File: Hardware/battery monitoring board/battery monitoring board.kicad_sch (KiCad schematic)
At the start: 1 part

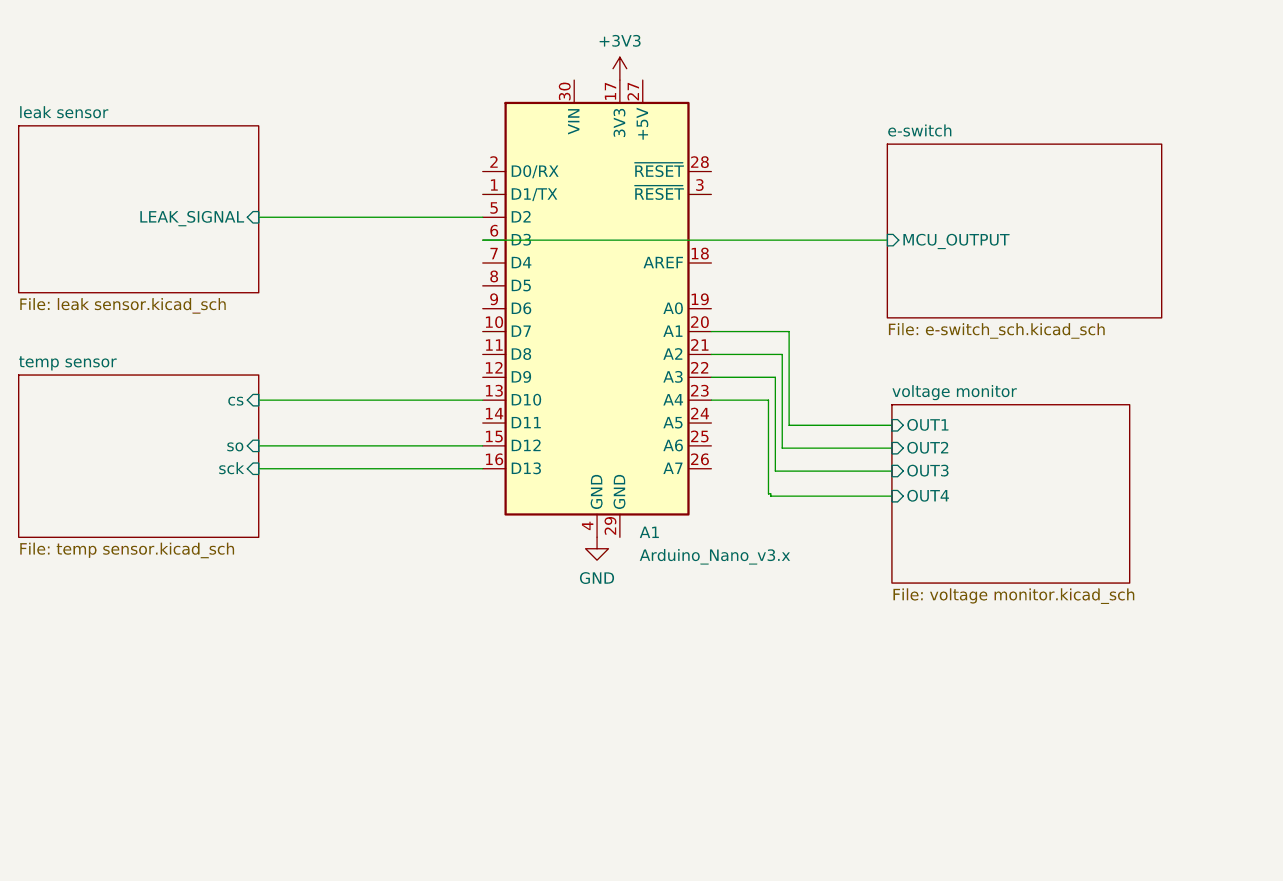
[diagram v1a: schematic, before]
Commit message: Added second battery monitor
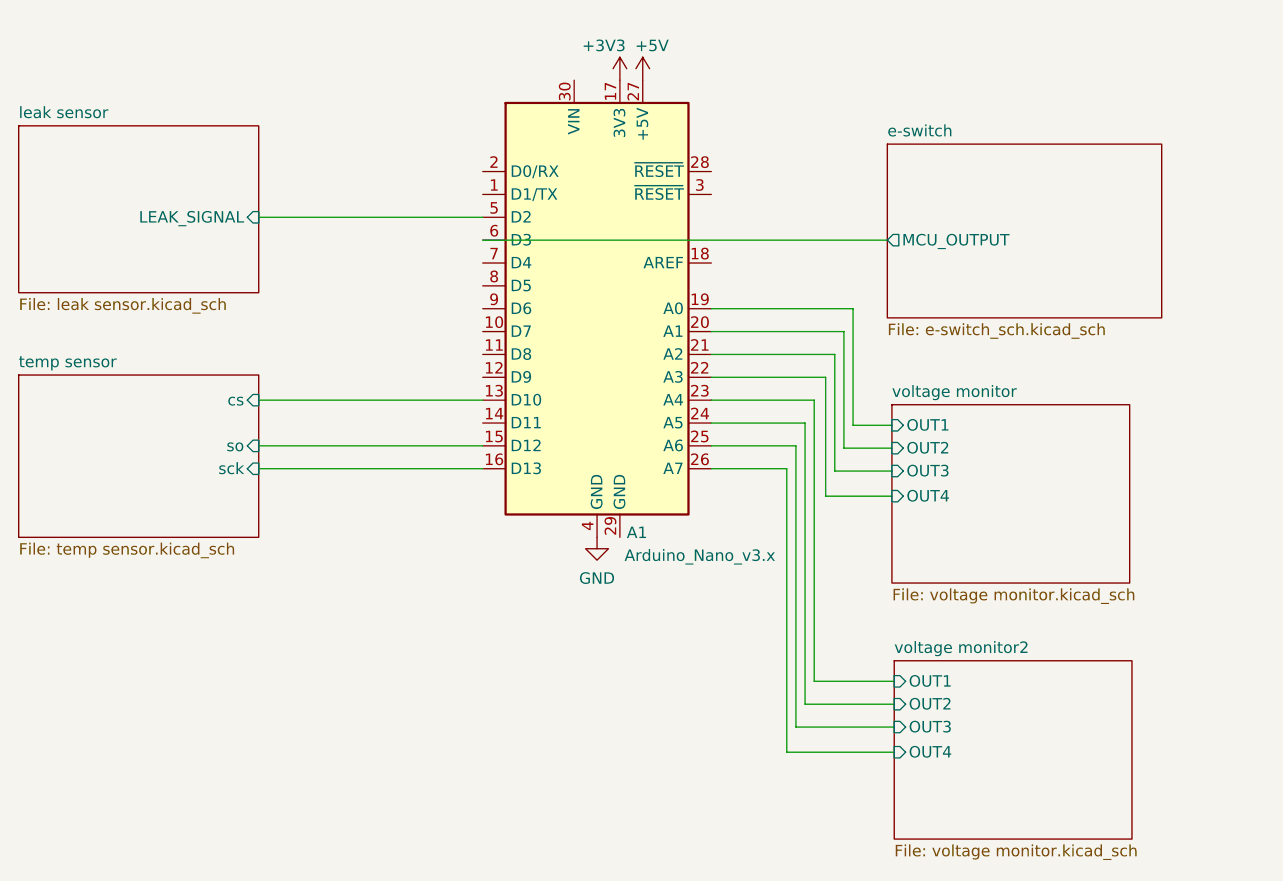
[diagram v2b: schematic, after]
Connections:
- net voltage monitor/OUT1: now also A1.19 (A0); no longer A1.20 (A1)
- net voltage monitor/OUT2: now also A1.20 (A1); no longer A1.21 (A2)
- net voltage monitor/OUT3: now also A1.21 (A2); no longer A1.22 (A3)
- net voltage monitor/OUT4: now also A1.22 (A3); no longer A1.23 (A4)
- net voltage monitor2/OUT2: now reaches A1.24 (A5)
- net voltage monitor2/OUT3: now reaches A1.25 (A6)
- net voltage monitor2/OUT4: now reaches A1.26 (A7)
- net +5V: now reaches A1.27 (+5V)
- new net voltage monitor2/OUT1: A1.23 (A4)
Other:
- added sheet voltage monitor2 (voltage monitor.kicad_sch)
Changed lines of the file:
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@@
 (kicad_sch (version 20230121) (generator eeschema)
   (paper "A4")
-  (wire (pts (xy 154.178 103.632) (xy 141.224 103.632))
+  (wire (pts (xy 148.844 88.138) (xy 134.112 88.138))
     (stroke (width 0) (type default))
   )
@@
     (stroke (width 0) (type default))
   )
-  (wire (pts (xy 140.462 106.172) (xy 140.462 95.758))
-    (stroke (width 0) (type default))
-  )
-  (wire (pts (xy 154.178 101.092) (xy 141.986 101.092))
-    (stroke (width 0) (type default))
-  )
-  (wire (pts (xy 141.986 101.092) (xy 141.986 90.678))
-    (stroke (width 0) (type default))
-  )
-  (wire (pts (xy 141.224 93.218) (xy 134.112 93.218))
-    (stroke (width 0) (type default))
-  )
-  (wire (pts (xy 140.716 106.426) (xy 154.178 106.426))
-    (stroke (width 0) (type default))
-  )
-  (wire (pts (xy 134.112 95.758) (xy 140.462 95.758))
+  (wire (pts (xy 149.86 85.598) (xy 149.86 98.552))
+    (stroke (width 0) (type default))
+  )
+  (wire (pts (xy 134.112 93.218) (xy 146.812 93.218))
+    (stroke (width 0) (type default))
+  )
+  (wire (pts (xy 147.828 90.678) (xy 147.828 103.632))
     (stroke (width 0) (type default))
   )
@@
     (stroke (width 0) (type default))
   )
-  (wire (pts (xy 154.178 98.552) (xy 142.748 98.552))
+  (wire (pts (xy 143.51 100.838) (xy 143.51 132.08))
     (stroke (width 0) (type default))
   )
@@
     (stroke (width 0) (type default))
   )
-  (wire (pts (xy 140.716 106.172) (xy 140.462 106.172))
-    (stroke (width 0) (type default))
-  )
-  (wire (pts (xy 141.224 103.632) (xy 141.224 93.218))
-    (stroke (width 0) (type default))
-  )
-  (wire (pts (xy 142.748 98.552) (xy 142.748 88.138))
-    (stroke (width 0) (type default))
-  )
-  (wire (pts (xy 140.716 106.172) (xy 140.716 106.426))
+  (wire (pts (xy 145.542 127) (xy 145.542 95.758))
+    (stroke (width 0) (type default))
+  )
+  (wire (pts (xy 148.844 101.092) (xy 148.844 88.138))
+    (stroke (width 0) (type default))
+  )
+  (wire (pts (xy 134.112 100.838) (xy 143.51 100.838))
+    (stroke (width 0) (type default))
+  )
+  (wire (pts (xy 134.112 98.298) (xy 144.526 98.298))
+    (stroke (width 0) (type default))
+  )
+  (wire (pts (xy 134.112 103.378) (xy 142.494 103.378))
+    (stroke (width 0) (type default))
+  )
+  (wire (pts (xy 134.112 90.678) (xy 147.828 90.678))
+    (stroke (width 0) (type default))
+  )
+  (wire (pts (xy 154.432 127) (xy 145.542 127))
+    (stroke (width 0) (type default))
+  )
+  (wire (pts (xy 147.828 103.632) (xy 154.178 103.632))
+    (stroke (width 0) (type default))
+  )
+  (wire (pts (xy 154.178 101.092) (xy 148.844 101.092))
+    (stroke (width 0) (type default))
+  )
+  (wire (pts (xy 146.812 106.426) (xy 154.178 106.426))
+    (stroke (width 0) (type default))
+  )
+  (wire (pts (xy 149.86 98.552) (xy 154.178 98.552))
+    (stroke (width 0) (type default))
+  )
+  (wire (pts (xy 144.526 129.54) (xy 154.432 129.54))
+    (stroke (width 0) (type default))
+  )
+  (wire (pts (xy 144.526 98.298) (xy 144.526 129.54))
+    (stroke (width 0) (type default))
+  )
+  (wire (pts (xy 146.812 93.218) (xy 146.812 106.426))
+    (stroke (width 0) (type default))
+  )
+  (wire (pts (xy 142.494 103.378) (xy 142.494 134.874))
+    (stroke (width 0) (type default))
+  )
+  (wire (pts (xy 134.112 85.598) (xy 149.86 85.598))
     (stroke (width 0) (type default))
   )
@@
     (stroke (width 0) (type default))
   )
-  (wire (pts (xy 142.748 88.138) (xy 134.112 88.138))
+  (wire (pts (xy 142.494 134.874) (xy 154.432 134.874))
     (stroke (width 0) (type default))
   )
@@
     (stroke (width 0) (type default))
   )
-  (wire (pts (xy 141.986 90.678) (xy 134.112 90.678))
+  (wire (pts (xy 134.112 95.758) (xy 145.542 95.758))
+    (stroke (width 0) (type default))
+  )
+  (wire (pts (xy 143.51 132.08) (xy 154.432 132.08))
     (stroke (width 0) (type default))
   )
   (symbol (lib_id "MCU_Module:Arduino_Nano_v3.x") (at 121.412 85.598 0) (unit 1)
-    (in_bom yes) (on_board yes) (dnp no) (fields_autoplaced)
-    (property "Reference" "A1" (at 126.1461 110.49 0)
-      (effects (font (size 1.27 1.27)) (justify left))
-    )
-    (property "Value" "Arduino_Nano_v3.x" (at 126.1461 113.03 0)
+    (in_bom yes) (on_board yes) (dnp no)
+    (property "Reference" "A1" (at 124.714 110.49 0)
+      (effects (font (size 1.27 1.27)) (justify left))
+    )
+    (property "Value" "Arduino_Nano_v3.x" (at 124.46 113.03 0)
       (effects (font (size 1.27 1.27)) (justify left))
     )
@@
     )
   )
+  (symbol (lib_id "power:+3V3") (at 123.952 60.198 0) (unit 1)
+    (in_bom yes) (on_board yes) (dnp no)
+    (property "Reference" "#PWR019" (at 123.952 64.008 0)
+      (effects (font (size 1.27 1.27)) hide)
+    )
+    (property "Value" "+3V3" (at 122.174 56.388 0)
+      (effects (font (size 1.27 1.27)))
+    )
+    (property "Footprint" "" (at 123.952 60.198 0)
+      (effects (font (size 1.27 1.27)) hide)
+    )
+    (property "Datasheet" "" (at 123.952 60.198 0)
+      (effects (font (size 1.27 1.27)) hide)
+    )
+    (pin "1")
+    (instances
+      (project "battery monitoring board"
+        (path "/bf623d80-ca5a-491f-9daa-4dffbeba5279"
+          (reference "#PWR019") (unit 1)
+        )
+      )
+    )
+  )
   (symbol (lib_id "PCM_4ms_Power-symbol:GND") (at 121.412 110.998 0) (unit 1)
     (in_bom yes) (on_board yes) (dnp no) (fields_autoplaced)
@@
     )
   )
-  (symbol (lib_id "power:+3V3") (at 123.952 60.198 0) (unit 1)
-    (in_bom yes) (on_board yes) (dnp no) (fields_autoplaced)
-    (property "Reference" "#PWR02" (at 123.952 64.008 0)
-      (effects (font (size 1.27 1.27)) hide)
-    )
-    (property "Value" "+3V3" (at 123.952 55.88 0)
+  (symbol (lib_id "PCM_4ms_Power-symbol:+5V") (at 126.492 60.198 0) (unit 1)
+    (in_bom yes) (on_board yes) (dnp no)
+    (property "Reference" "#PWR02" (at 126.492 64.008 0)
+      (effects (font (size 1.27 1.27)) hide)
+    )
+    (property "Value" "+5V" (at 127.508 56.388 0)
       (effects (font (size 1.27 1.27)))
     )
-    (property "Footprint" "" (at 123.952 60.198 0)
-      (effects (font (size 1.27 1.27)) hide)
-    )
-    (property "Datasheet" "" (at 123.952 60.198 0)
+    (property "Footprint" "" (at 126.492 60.198 0)
+      (effects (font (size 1.27 1.27)) hide)
+    )
+    (property "Datasheet" "" (at 126.492 60.198 0)
       (effects (font (size 1.27 1.27)) hide)
     )
@@
     )
   )
+  (sheet (at 154.432 124.714) (size 26.416 19.812) (fields_autoplaced)
+    (stroke (width 0.1524) (type solid))
+    (fill (color 0 0 0 0.0000))
+    (property "Sheetname" "voltage monitor2" (at 154.432 124.0024 0)
+      (effects (font (size 1.27 1.27)) (justify left bottom))
+    )
+    (property "Sheetfile" "voltage monitor.kicad_sch" (at 154.432 145.1106 0)
+      (effects (font (size 1.27 1.27)) (justify left top))
+    )
+    (pin "OUT4" input (at 154.432 134.874 180)
+      (effects (font (size 1.27 1.27)) (justify left))
+    )
+    (pin "OUT3" input (at 154.432 132.08 180)
+      (effects (font (size 1.27 1.27)) (justify left))
+    )
+    (pin "OUT2" input (at 154.432 129.54 180)
+      (effects (font (size 1.27 1.27)) (justify left))
+    )
+    (pin "OUT1" input (at 154.432 127 180)
+      (effects (font (size 1.27 1.27)) (justify left))
+    )
+    (instances
+      (project "battery monitoring board"
+        (path "/bf623d80-ca5a-491f-9daa-4dffbeba5279" (page "6"))
+      )
+    )
+  )
   (sheet (at 57.15 92.964) (size 26.67 18.034) (fields_autoplaced)
     (stroke (width 0.1524) (type solid))
@@
       (effects (font (size 1.27 1.27)) (justify left top))
     )
-    (pin "MCU_OUTPUT" input (at 153.67 77.978 180)
-      (effects (font (size 1.27 1.27)) (justify left))
-    )
+    (pin "MCU_OUTPUT" output (at 153.67 77.978 180)
+      (effects (font (size 1.27 1.27)) (justify left))
+    )

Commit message: Update voltage divider
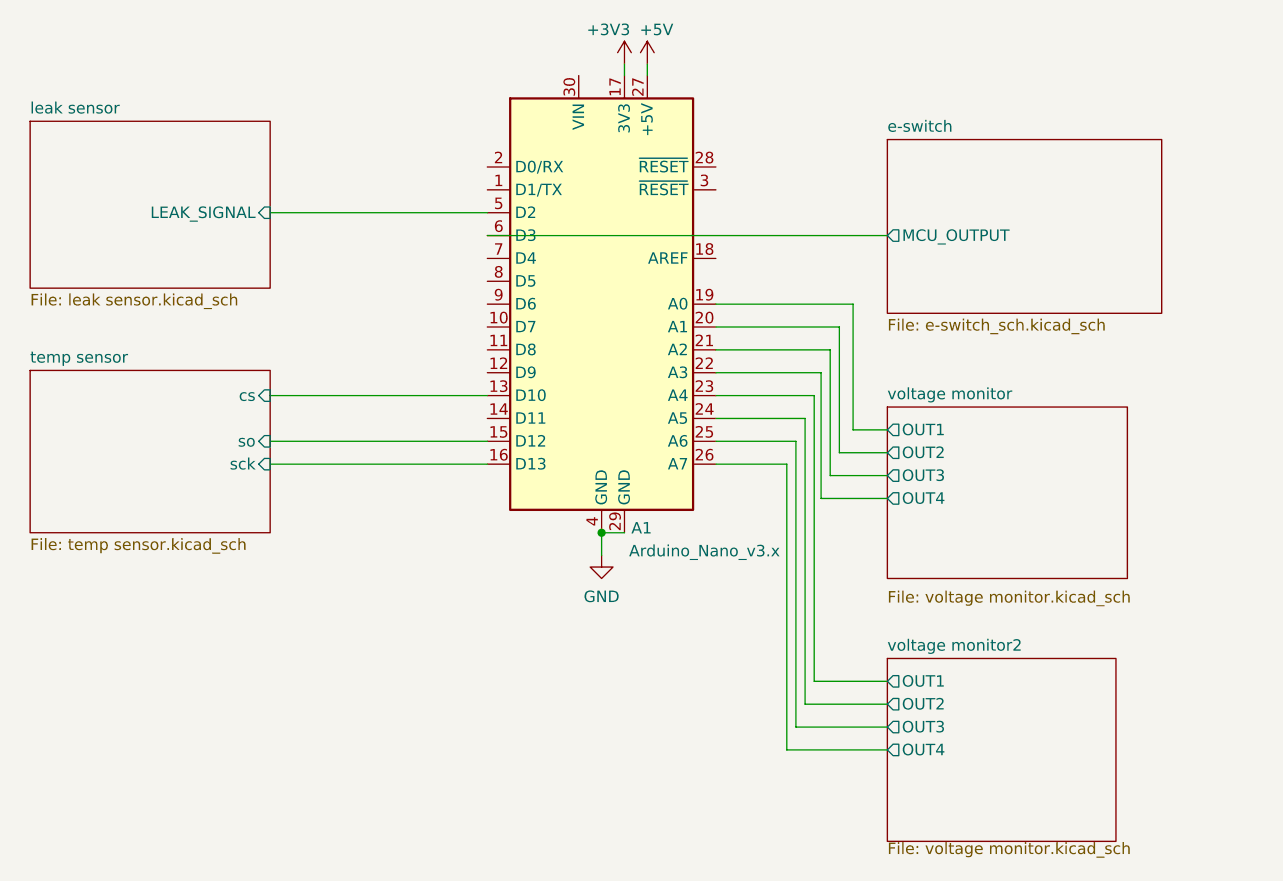
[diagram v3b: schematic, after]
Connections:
- net GND: now also A1.29 (GND)
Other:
- moved on the sheet: A1
